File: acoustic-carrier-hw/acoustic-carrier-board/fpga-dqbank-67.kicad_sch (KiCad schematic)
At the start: 11 parts, among them IC1 ECP5-BGA256, Y602 Crystal Oscillator

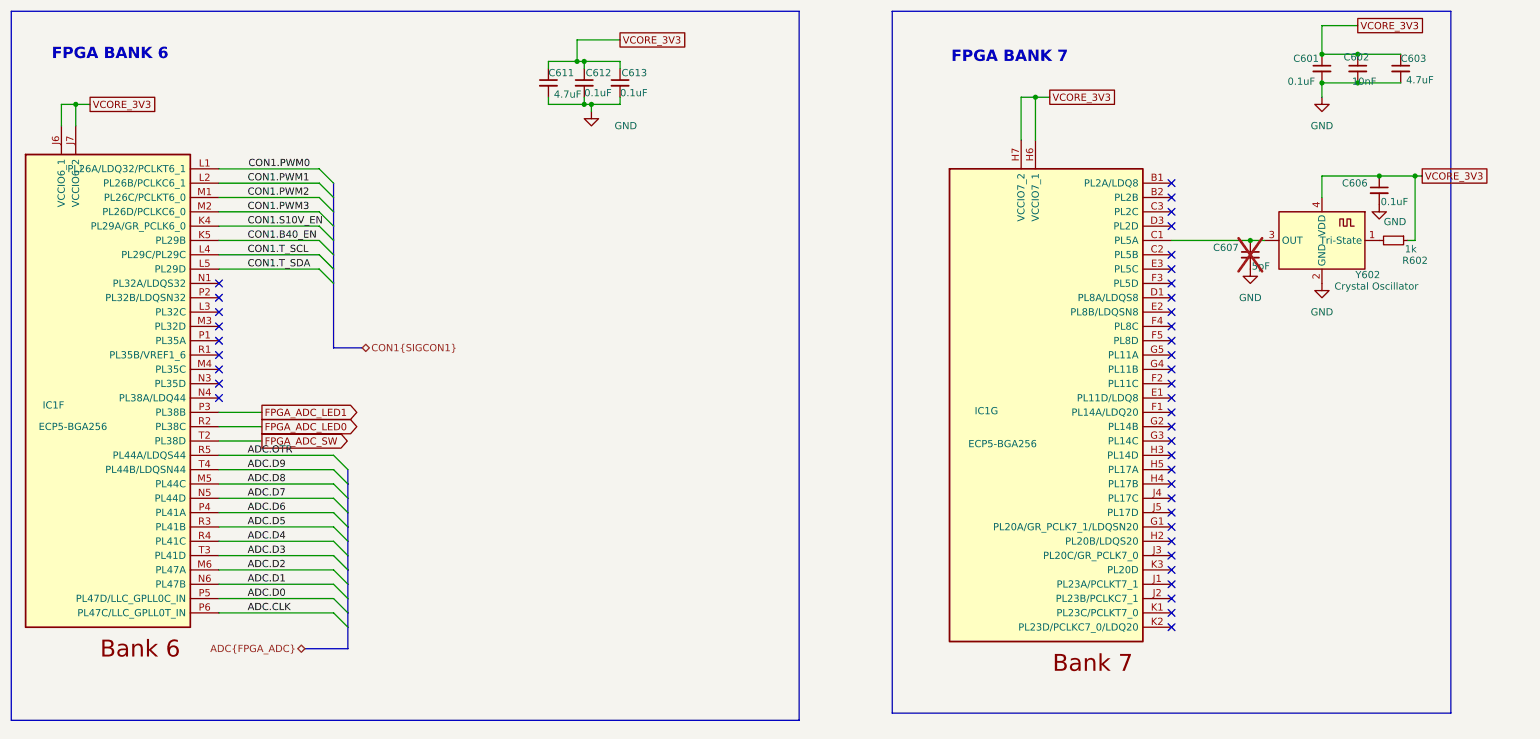
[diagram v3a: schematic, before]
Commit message: [¢arrier] Placed power supply circuitry appropraitely, changed power connector (next) Place schmitt triggers between usb and power, put critical circuitry closer together, place config circuitry
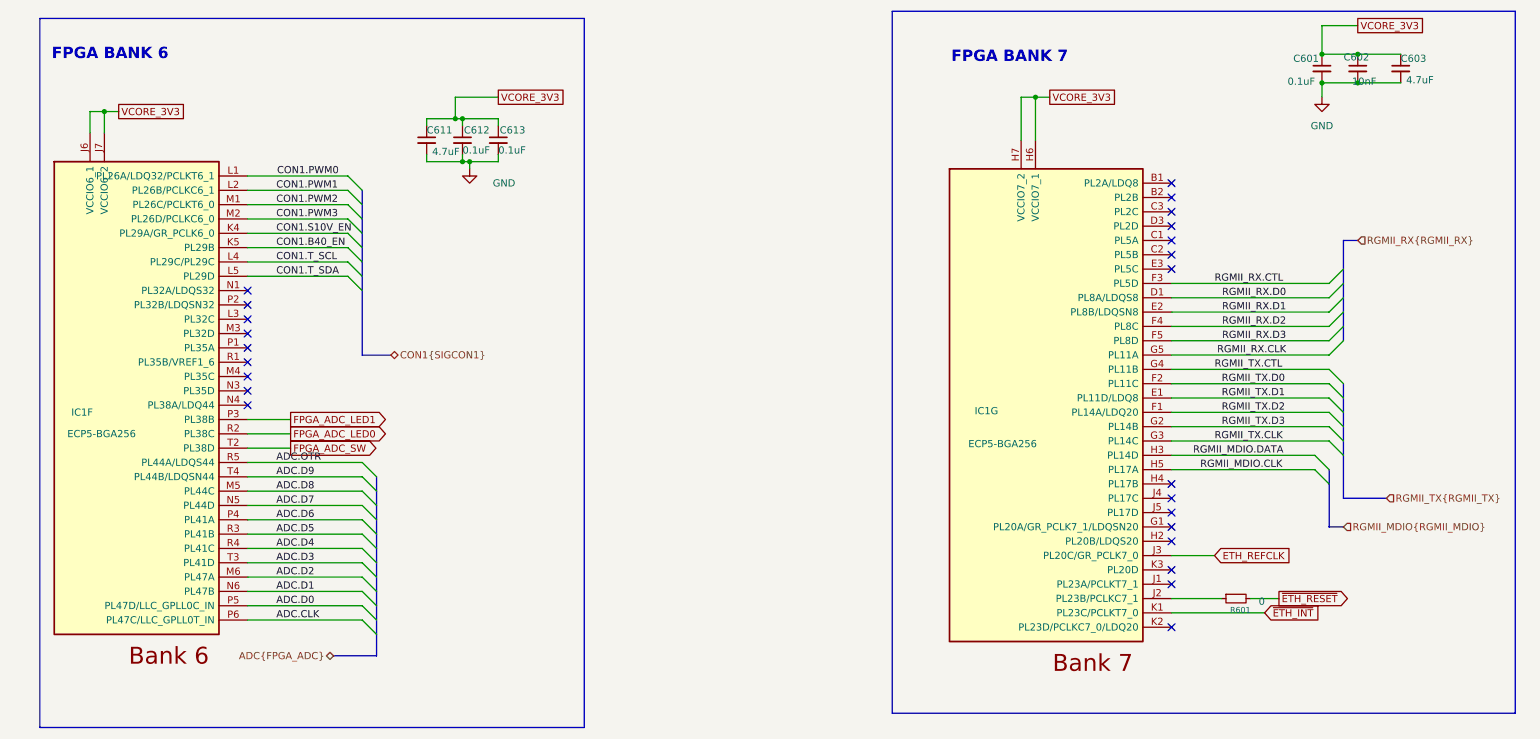
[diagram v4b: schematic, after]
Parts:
- removed C606: 0.1uF, Capacitor_SMD:C_0201_0603Metric, symbol Device:C_Small
- removed C607: 5pF, Capacitor_SMD:C_0603_1608Metric, symbol Device:C_Small
- removed R602: 1k, Resistor_SMD:R_0603_1608Metric, symbol Device:R_Small
- removed Y602: Crystal Oscillator, Crystal:Crystal_SMD_3225-4Pin_3.2x2.5mm, symbol Oscillator:ASCO
- added R601: 0, Resistor_SMD:R_0603_1608Metric, symbol Device:R_Small
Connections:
- net RGMII_RX.D0: now reaches IC1.D1 (PL8A/LDQS8)
- net RGMII_TX.D1: now reaches IC1.E1 (PL11D/LDQ8)
- net RGMII_RX.D1: now reaches IC1.E2 (PL8B/LDQSN8)
- net RGMII_TX.D2: now reaches IC1.F1 (PL14A/LDQ20)
- net RGMII_TX.D0: now reaches IC1.F2 (PL11C)
- net RGMII_RX.CTL: now reaches IC1.F3 (PL5D)
- net RGMII_RX.D2: now reaches IC1.F4 (PL8C)
- net RGMII_RX.D3: now reaches IC1.F5 (PL8D)
- net RGMII_TX.D3: now reaches IC1.G2 (PL14B)
- net RGMII_TX.CLK: now reaches IC1.G3 (PL14C)
- net RGMII_TX.CTL: now reaches IC1.G4 (PL11B)
- net RGMII_RX.CLK: now reaches IC1.G5 (PL11A)
- net RGMII_MDIO.DATA: now reaches IC1.H3 (PL14D)
- net RGMII_MDIO.CLK: now reaches IC1.H5 (PL17A)
- net at IC1.J2 (PL23B/PCLKC7_1): now also R601.1
- net ETH_REFCLK: now reaches IC1.J3 (PL20C/GR_PCLK7_0)
- net ~{ETH_INT}: now reaches IC1.K1 (PL23C/PCLKT7_0)
- new net ~{ETH_RESET}: R601.2
- no-connect marks 40 -> 24
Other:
- moved on the sheet: C611, C612, C613, IC1F
